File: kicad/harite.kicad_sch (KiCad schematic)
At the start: 78 parts, among them J1 503480-0500, J2 Wired Joystick, J4 5034801200, J5 5034801200, U1 RP2040_Zero, U2 RP2040_Zero

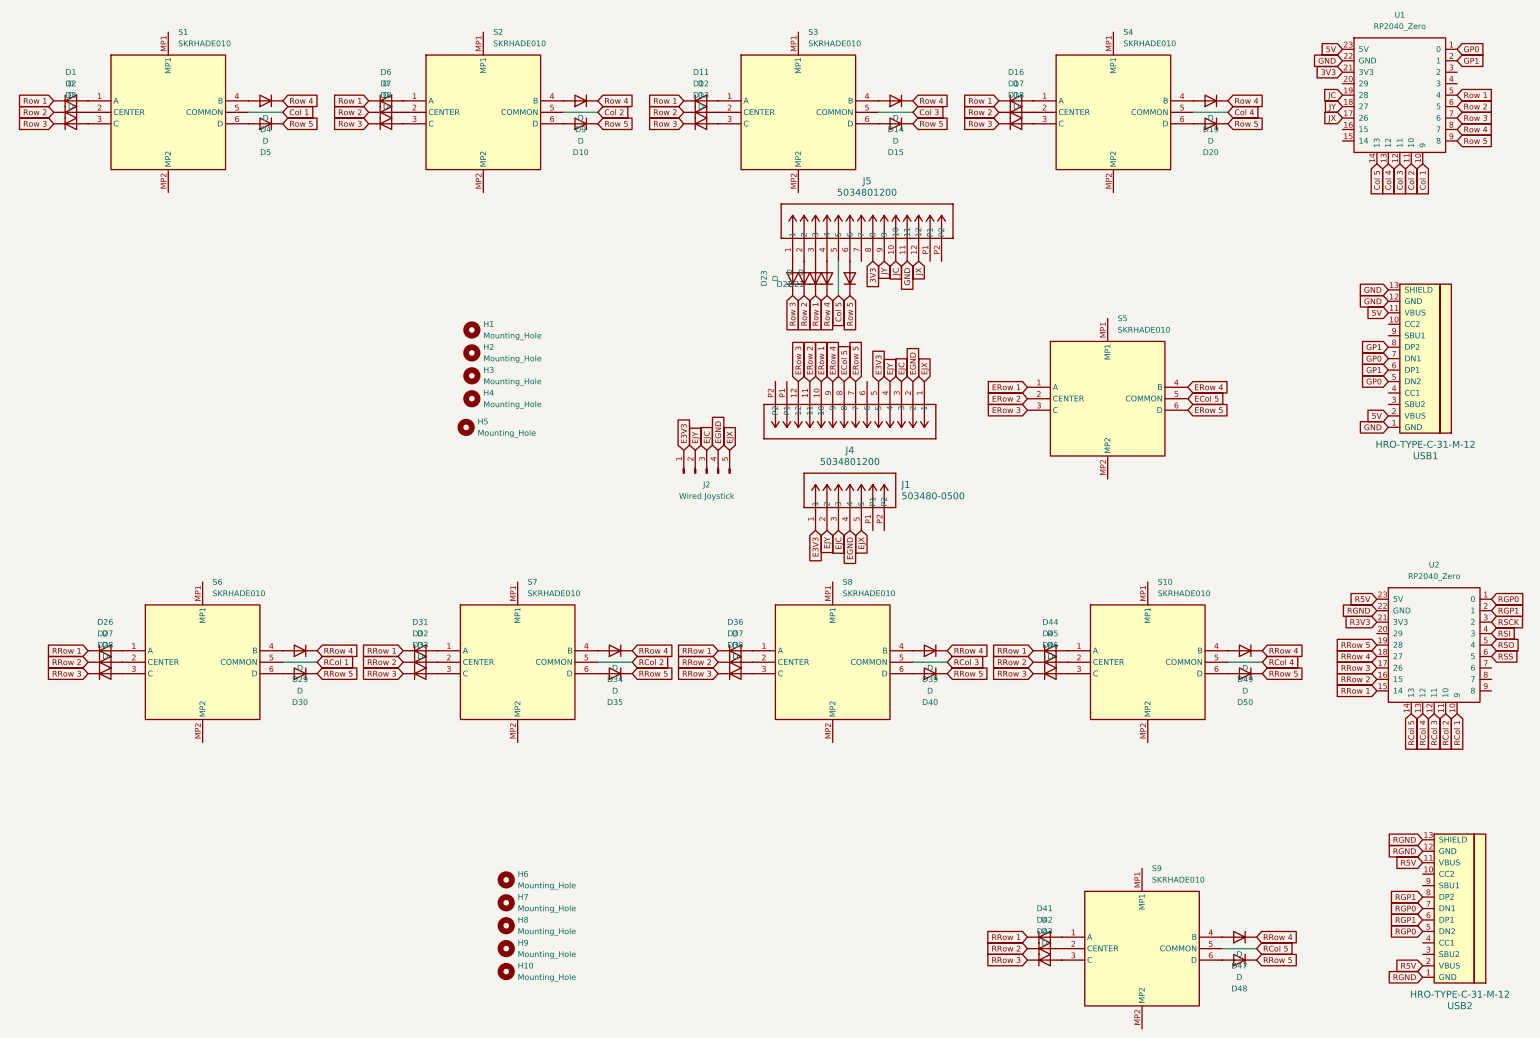
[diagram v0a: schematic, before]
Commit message: Change to ps5 joystick
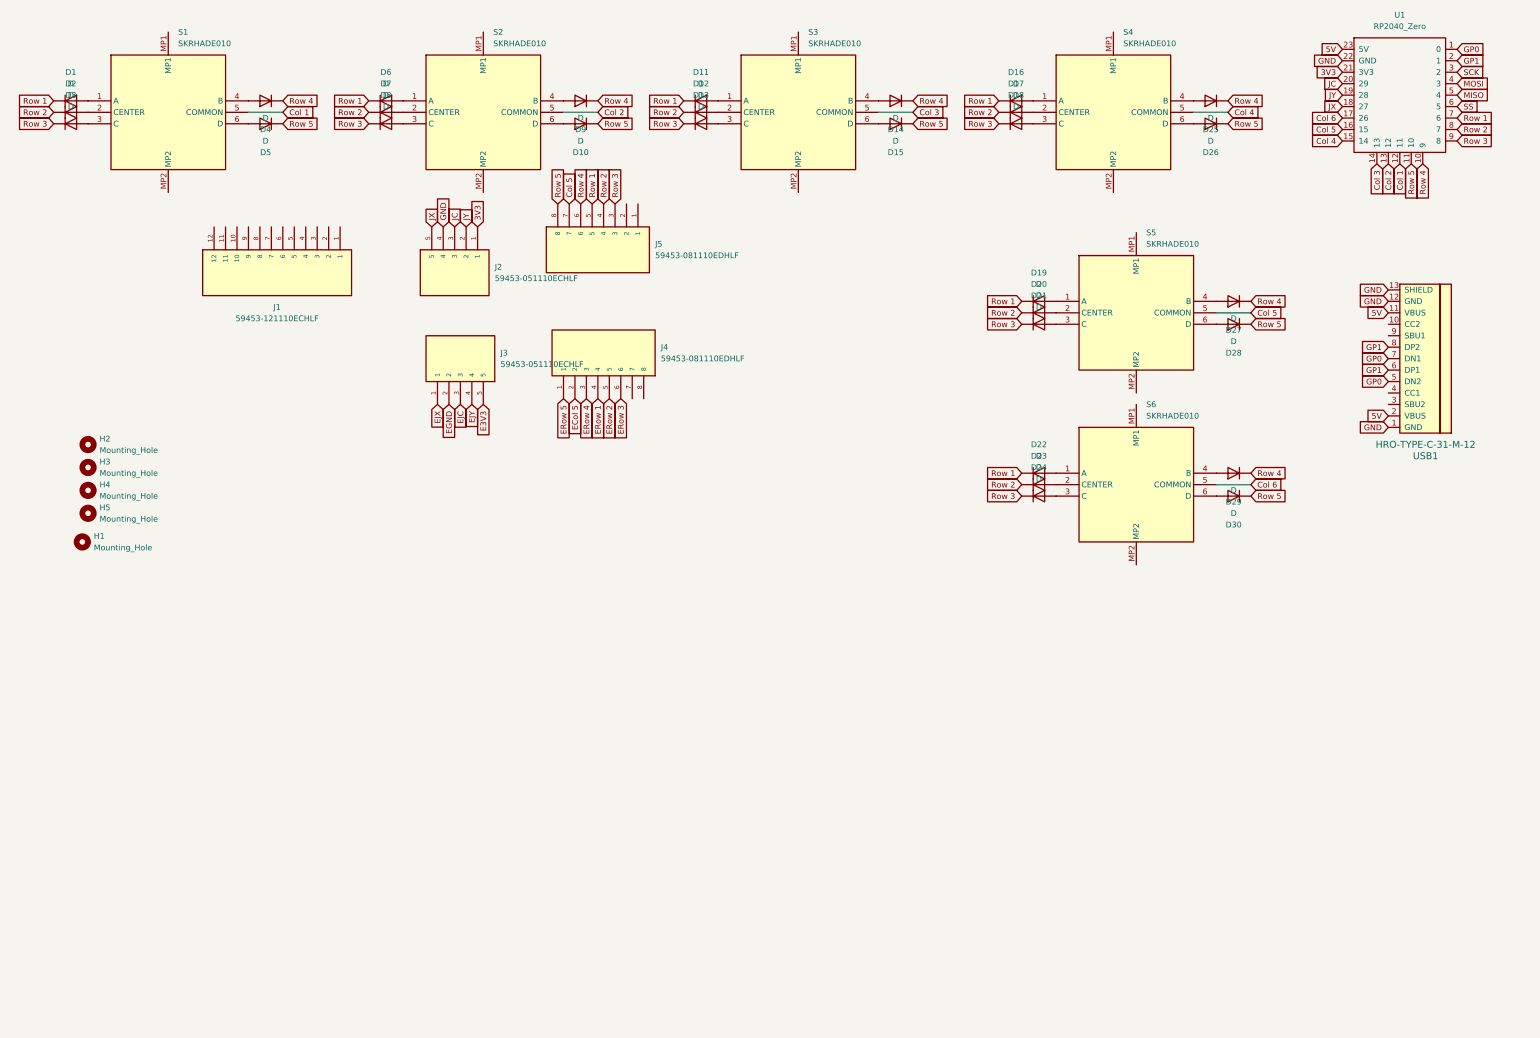
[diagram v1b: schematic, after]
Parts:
- removed D25, D26, D31, D32, D33, D34, D35, D36, D37, D38, D39, D40, D41, D42, D43, D44, D45, D46, D47, D48, D49, D50: D, ScottoKeebs_Components:Diode_SOD-123, symbol Device:D
- removed H10, H6, H7, H8, H9: Mounting_Hole, MountingHole:MountingHole_2.2mm_M2_Pad_Via, symbol ScottoKeebs:Placeholder_Mounting_Hole
- removed J1: 503480-0500, 5034800540, symbol 5034800540:5034800540
- removed J2: Wired Joystick, Wired-Joystick, symbol Connector:Conn_01x05_Pin
- removed J4, J5: 5034801200, 5034801200, symbol 5034801200:5034801200
- removed S10, S7, S8, S9: SKRHADE010, footprints:SKRHADE, symbol SKRHADE010:SKRHADE010
- removed U2: RP2040_Zero, ScottoKeebs_MCU:RP2040_Zero, symbol ScottoKeebs:MCU_RP2040_Zero
- removed USB2: HRO-TYPE-C-31-M-12, footprints:HRO-TYPE-C-31-M-12, symbol USBType-C:HRO-TYPE-C-31-M-12
- added D19, D20: D, ScottoKeebs_Components:Diode_SOD-123, symbol Device:D
- added J1: 59453-121110ECHLF, AMPHENOL_59453-121110ECHLF, symbol 59453-121110ECHLF:59453-121110ECHLF
- added J2, J3: 59453-051110ECHLF, AMPHENOL_59453-051110ECHLF, symbol 59453-051110ECHLF:59453-051110ECHLF
- added J4, J5: 59453-081110EDHLF, AMPHENOL_59453-081110EDHLF, symbol 59453-081110EDHLF:59453-081110EDHLF
- S1, S2, S3, S4, S5, S6: footprint footprints:SKRHADE -> SKRHADE010
- renumbered D19 to D25, D20 to D26
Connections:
- net RRow 2 is gone; now on net Row 4: D27.1 (K)
- net RRow 3 is gone; now on net Row 5: D28.1 (K)
- net RRow 4 is gone; now on net Row 4: D29.1 (K)
- net RRow 5 is gone; now on net Row 5: D30.1 (K)
- net 3V3: now also J2.1
- net Col 1: now also U1.12 (11); no longer U1.10 (9)
- net Col 2: now also U1.13 (12); no longer U1.11 (10)
- net Col 3: now also U1.14 (13); no longer U1.12 (11)
- net Col 4: now also U1.15 (14); no longer U1.13 (12)
- net Col 5: now also S5.5 (COMMON), U1.16 (15), J5.7; no longer U1.14 (13)
- net E3V3: now also J3.5
- net ECol 5: now also J4.2; no longer S5.5 (COMMON)
- net EGND: now also J3.2
- net EJC: now also J3.3
- net EJX: now also J3.1
- net EJY: now also J3.4
- net ERow 1: now also J4.4; no longer S5.1 (A)
- net ERow 2: now also J4.5; no longer S5.2 (CENTER)
- net ERow 3: now also J4.6; no longer S5.3 (C)
- net ERow 4: now also J4.3; no longer S5.4 (B)
- net ERow 5: now also J4.1; no longer S5.6 (D)
- net GND: now also J2.4
- net JC: now also U1.20 (29), J2.3; no longer U1.19 (28)
- net JX: now also U1.18 (27), J2.5; no longer U1.17 (26)
- net JY: now also U1.19 (28), J2.2; no longer U1.18 (27)
- net Row 1: now also D22.1 (K), U1.7 (6), D19.1 (K), J5.5; no longer D21.1 (K), U1.5 (4)
- net Row 2: now also D23.1 (K), U1.8 (7), D20.1 (K), J5.4; no longer D22.1 (K), U1.6 (5)
- net Row 3: now also D21.1 (K), D24.1 (K), U1.9 (8), J5.3; no longer D23.1 (K), U1.7 (6)
- net Row 4: now also U1.10 (9), J5.6; no longer D24.1 (K), U1.8 (7)
- net Row 5: now also U1.11 (10), J5.8; no longer U1.9 (8)
- net at D24.2 (A): now also S6.3 (C)
- net at D23.2 (A): now also S6.2 (CENTER)
- net at D22.2 (A): now also S6.1 (A)
- net at D27.2 (A): now also S5.4 (B); no longer S6.2 (CENTER)
- net SCK: now reaches U1.3 (2)
- net MOSI: now reaches U1.4 (3)
- net at D21.2 (A): now also S5.3 (C)
- net at D28.2 (A): now also S5.6 (D); no longer S6.3 (C)
- net RCol 1 renamed Col 6
- net Col 6: now also U1.17 (26)
- new net: D20.2 (A), S5.2 (CENTER)
- new net: D19.2 (A), S5.1 (A)
- new net MISO: U1.5 (4)
- new net SS: U1.6 (5)

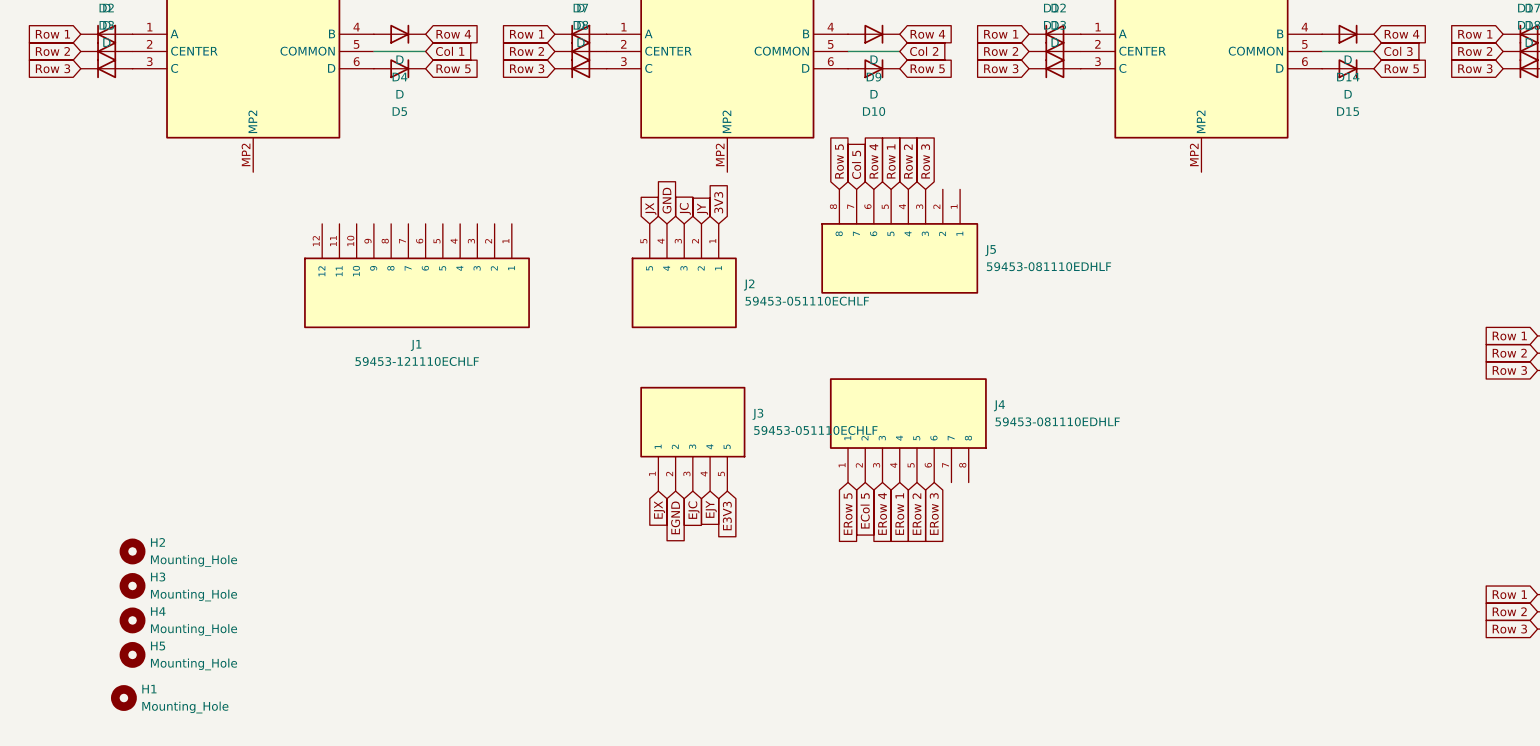
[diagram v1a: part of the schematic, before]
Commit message: fix footprints
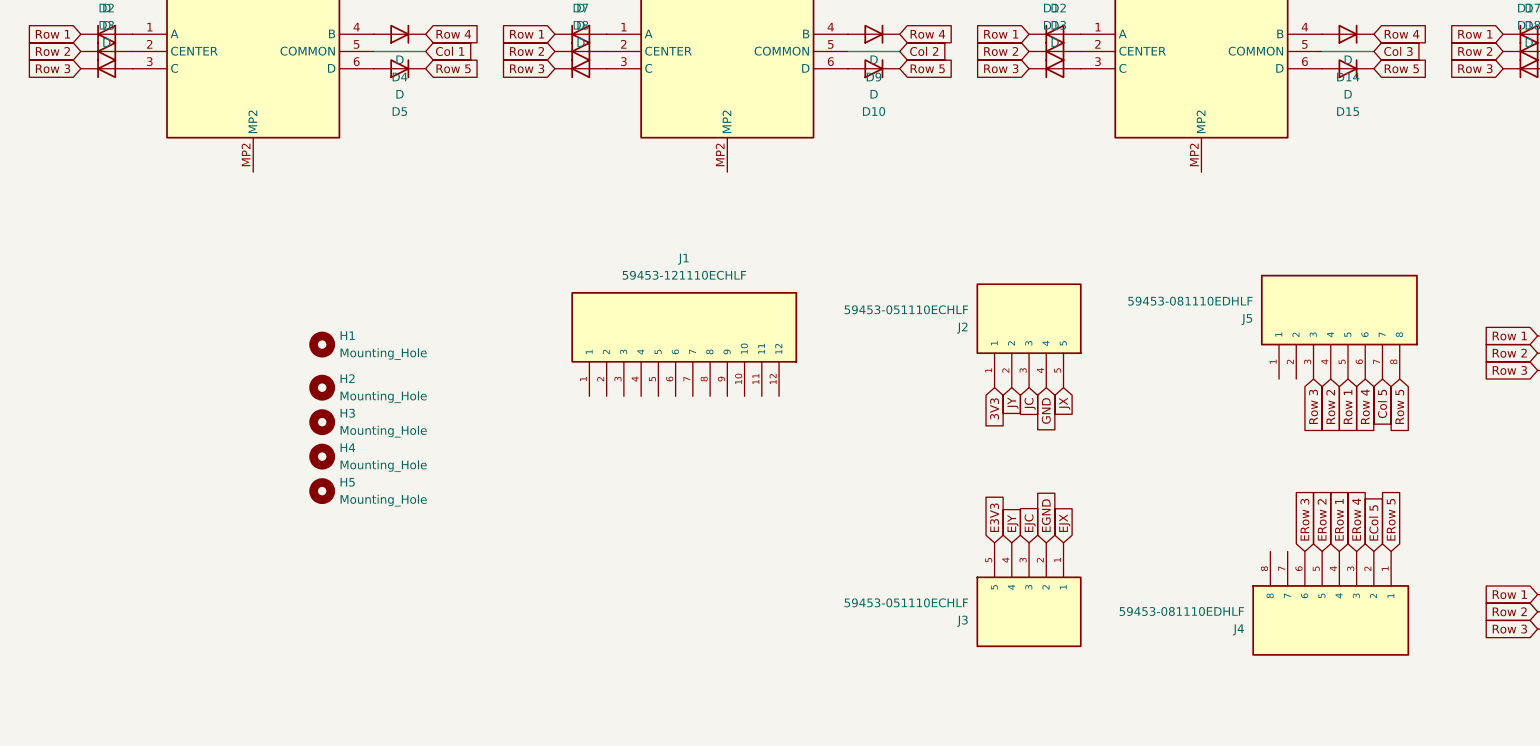
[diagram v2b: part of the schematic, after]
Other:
- moved on the sheet: H1, H2, H3, H4, H5, J1, J2, J3, J4, J5

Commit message: Update nets
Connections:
- net 3V3: now also J1.1
- net Col 5: no longer S5.5 (COMMON)
- net Col 6: now also J5.2; no longer S6.5 (COMMON)
- net ECol 5: now also S5.5 (COMMON)
- net ERow 1: now also D19.1 (K), D22.1 (K)
- net ERow 2: now also D20.1 (K), D23.1 (K)
- net ERow 3: now also D21.1 (K), D24.1 (K)
- net ERow 4: now also D27.1 (K), D29.1 (K)
- net ERow 5: now also D28.1 (K), D30.1 (K)
- net GND: now also J1.2
- net MISO: now also J1.11
- net MOSI: now also J1.8
- net Row 1: no longer D19.1 (K), D22.1 (K)
- net Row 2: no longer D20.1 (K), D23.1 (K)
- net Row 3: no longer D21.1 (K), D24.1 (K)
- net Row 4: no longer D27.1 (K), D29.1 (K)
- net Row 5: no longer D28.1 (K), D30.1 (K)
- net SCK: now also J1.12
- net SS: now also J1.10
- net ECol 6: now reaches J4.7
- net ECol 6: now also S6.5 (COMMON)
